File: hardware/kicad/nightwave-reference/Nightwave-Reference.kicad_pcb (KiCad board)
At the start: 4 copper layers, 110 x 100 mm, 61 parts, among them J1 USB4105-GF-A, J2 BATTERY_1S_10050mAh, J3 EXTERNAL_10K_NTC, J4 Molex 104031-0811, J5 SJ-3523-SMT-TR, J6 CMS-28528N-L152, J7 Waveshare 24382 TFT, J8 UART0_SERVICE, SW1 PREV, SW2 PLAY_PAUSE, SW3 NEXT, SW4 VOL_DOWN, SW5 VOL_UP, SW6 MAIN_POWER, U1 ESP32-S3-WROOM-1-N16R8, U10 MAX98357AETE+T, U11 TCA9535PWR, U12 BM83SM1-00TA, U2 TUSB320LAIRWBR, U3 BQ25628ERYKR, U4 TPS22965DSGR, U5 TPS63802DLAR, U6 TPS63802DLAR, U7 MAX17048G+T10, U8 PCM5102APWR, U9 TPA6132A2RTER

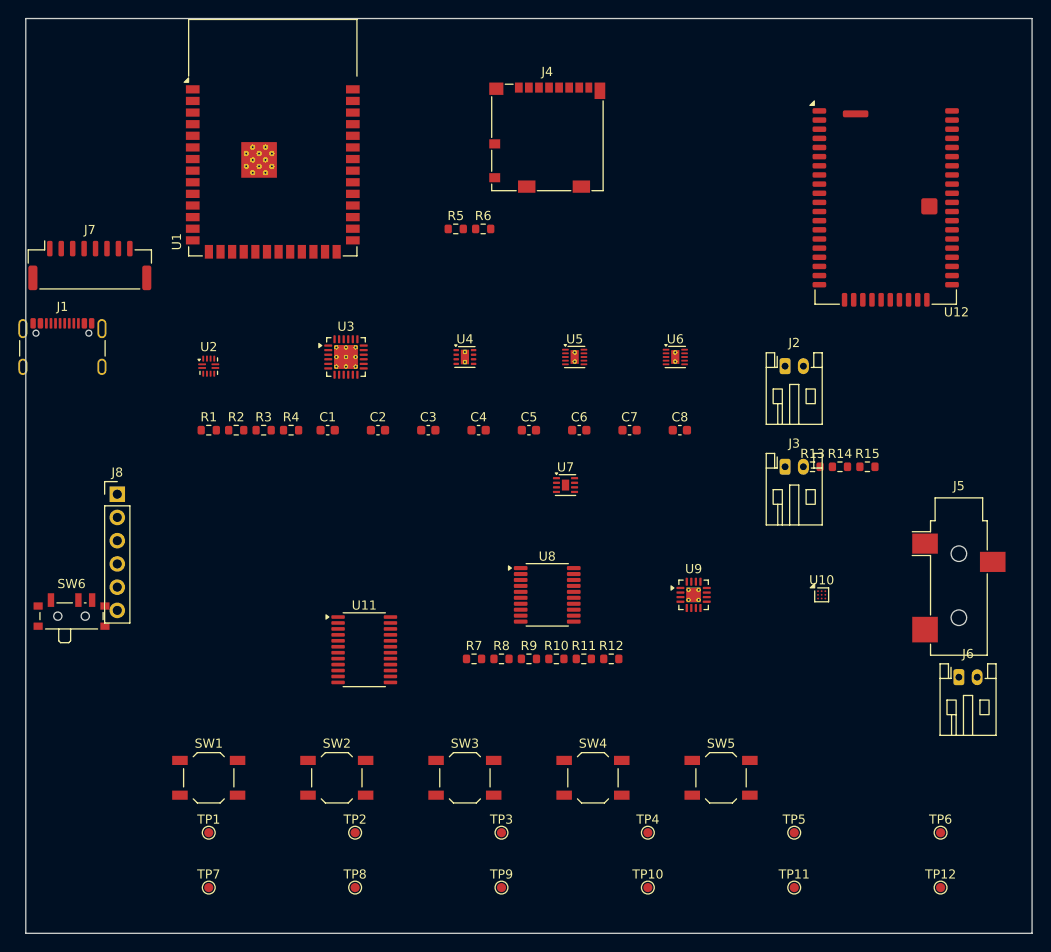
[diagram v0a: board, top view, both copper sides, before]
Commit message: hardware: close reference PCB routing and verify CAD exports
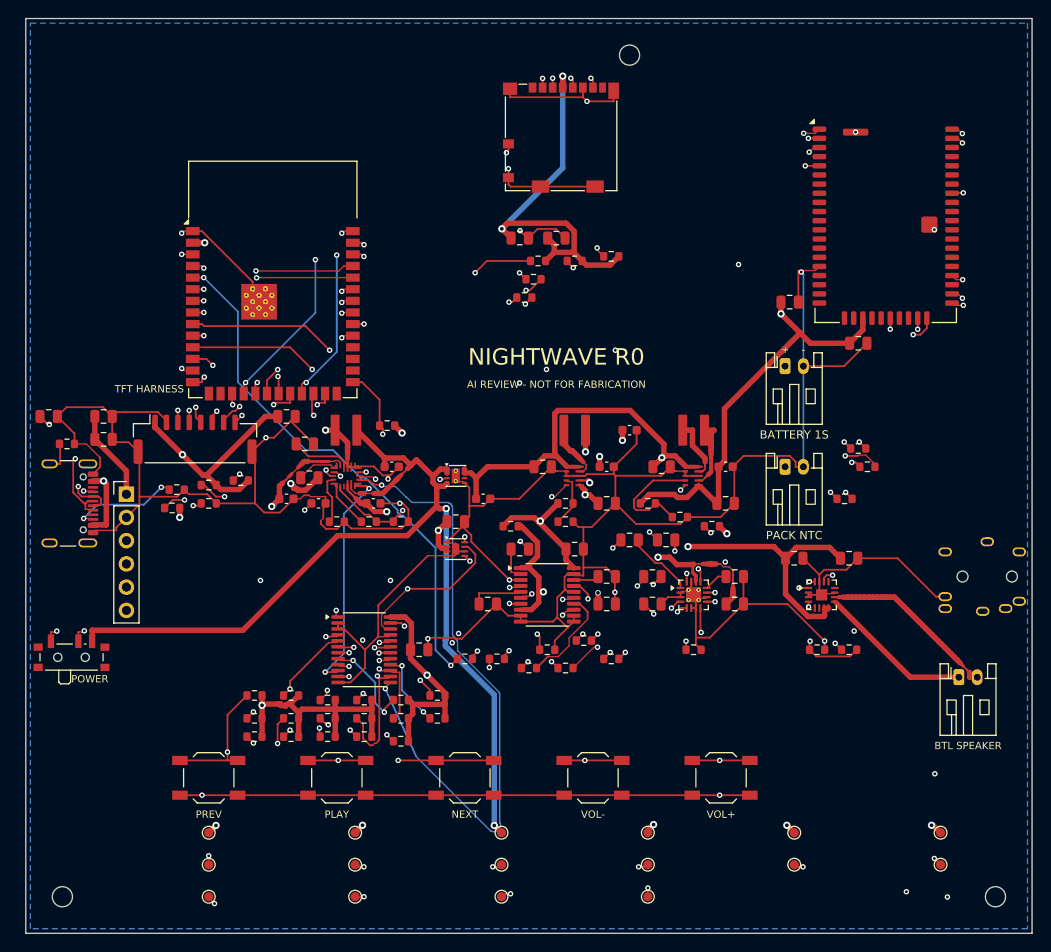
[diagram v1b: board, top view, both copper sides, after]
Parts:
- removed U2: TUSB320LAIRWBR, Package_DFN_QFN:Texas_X2QFN-12_1.6x1.6mm_P0.4mm
- added C10: 10u/25V, Capacitor_SMD:C_0805_2012Metric, F.Cu at (35.5, 51.5)
- added C11: 10u/10V, Capacitor_SMD:C_0805_2012Metric, F.Cu at (61.5, 54.0)
- added C12: 22u/10V, Capacitor_SMD:C_0805_2012Metric, F.Cu at (68.5, 58.0)
- added C13: 10u/10V, Capacitor_SMD:C_0805_2012Metric, F.Cu at (74.5, 54.0)
- added C14: 22u/10V, Capacitor_SMD:C_0805_2012Metric, F.Cu at (81.5, 58.0)
- added C15: 100n/10V, Capacitor_SMD:C_0805_2012Metric, F.Cu at (52.0, 60.0)
- added C16: 100n/10V, Capacitor_SMD:C_0805_2012Metric, F.Cu at (13.5, 51.0)
- added C17: 10u/10V, Capacitor_SMD:C_0805_2012Metric, F.Cu at (13.5, 48.5)
- added C18: 1u/10V, Capacitor_SMD:C_0805_2012Metric, F.Cu at (7.50, 48.5)
- added C19: 100n/10V, Capacitor_SMD:C_0805_2012Metric, F.Cu at (59.0, 29.0)
- added C20: 10u/10V, Capacitor_SMD:C_0805_2012Metric, F.Cu at (63.0, 29.0)
- added C21: 2.2u/10V, Capacitor_SMD:C_0805_2012Metric, F.Cu at (59.0, 63.0)
- added C22: 2.2u/10V, Capacitor_SMD:C_0805_2012Metric, F.Cu at (55.5, 69.0)
- added C23: 100n/10V, Capacitor_SMD:C_0805_2012Metric, F.Cu at (68.5, 66.0)
- added C24: 100n/10V, Capacitor_SMD:C_0805_2012Metric, F.Cu at (68.5, 69.0)
- added C25: 100n/10V, Capacitor_SMD:C_0805_2012Metric, F.Cu at (65.0, 63.0)
- added C26: 1u/10V, Capacitor_SMD:C_0805_2012Metric, F.Cu at (73.5, 66.0)
- added C27: 1u/10V, Capacitor_SMD:C_0805_2012Metric, F.Cu at (73.5, 69.0)
- added C28: 2.2u/10V, Capacitor_SMD:C_0805_2012Metric, F.Cu at (82.5, 66.0)
- added C29: 1u/10V, Capacitor_SMD:C_0805_2012Metric, F.Cu at (71.0, 62.0)
- added C30: 1u/10V, Capacitor_SMD:C_0805_2012Metric, F.Cu at (75.0, 62.0)
- added C31: 100n/10V, Capacitor_SMD:C_0805_2012Metric, F.Cu at (82.5, 69.0)
- added C32: 100n/10V, Capacitor_SMD:C_0805_2012Metric, F.Cu at (89.0, 64.0)
- added C33: 10u/10V, Capacitor_SMD:C_0805_2012Metric, F.Cu at (95.0, 64.0)
- added C34: 100n/10V, Capacitor_SMD:C_0805_2012Metric, F.Cu at (48.0, 74.0)
- added C35: 10u/10V, Capacitor_SMD:C_0805_2012Metric, F.Cu at (33.5, 48.5)
- added C36: 10u/10V, Capacitor_SMD:C_0805_2012Metric, F.Cu at (88.5, 36.0)
- added C37: 100n/10V, Capacitor_SMD:C_0805_2012Metric, F.Cu at (96.0, 40.5)
- added C9: 47n/10V, Capacitor_SMD:C_0805_2012Metric, F.Cu at (36.0, 55.2)
- added H1: M2_NPTH_NYLON_HARDWARE, MountingHole:MountingHole_2.2mm_M2, F.Cu at (71.0, 9.00)
- added H2: M2_NPTH_NYLON_HARDWARE, MountingHole:MountingHole_2.2mm_M2, F.Cu at (9.00, 101.0)
- added H3: M2_NPTH_NYLON_HARDWARE, MountingHole:MountingHole_2.2mm_M2, F.Cu at (111.0, 101.0)
- added L1: 0.47uH XFL4015-471MEC, Nightwave:Coilcraft_XFL4015, F.Cu at (65.0, 50.0)
- added L2: 0.47uH XFL4015-471MEC, Nightwave:Coilcraft_XFL4015, F.Cu at (78.0, 50.0)
- added L3: 0.7uH XFL4015-701MEC, Nightwave:Coilcraft_XFL4015, F.Cu at (40.0, 50.0)
- added R16: 511k, Resistor_SMD:R_0603_1608Metric, F.Cu at (64.0, 58.0)
- added R17: 91k, Resistor_SMD:R_0603_1608Metric, F.Cu at (64.0, 60.0)
- added R18: 562k, Resistor_SMD:R_0603_1608Metric, F.Cu at (73.0, 58.0)
- added R19: 91k, Resistor_SMD:R_0603_1608Metric, F.Cu at (76.5, 59.5)
- added R20: 5.49k, Resistor_SMD:R_0603_1608Metric, F.Cu at (39.0, 60.0)
- added R21: 5.23k, Resistor_SMD:R_0603_1608Metric, F.Cu at (42.5, 60.0)
- added R22: 30.1k, Resistor_SMD:R_0603_1608Metric, F.Cu at (46.0, 60.0)
- added R23: 0, Resistor_SMD:R_0603_1608Metric, F.Cu at (9.50, 51.5)
- added R24: 10k, Resistor_SMD:R_0603_1608Metric, F.Cu at (21.0, 58.5)
- added R25: 10k, Resistor_SMD:R_0603_1608Metric, F.Cu at (44.5, 49.5)
- added R26: 10k, Resistor_SMD:R_0603_1608Metric, F.Cu at (80.0, 60.5)
- added R27: 10k, Resistor_SMD:R_0603_1608Metric, F.Cu at (91.5, 74.0)
- added R28: 10k, Resistor_SMD:R_0603_1608Metric, F.Cu at (78.0, 74.0)
- added R29: 10k, Resistor_SMD:R_0603_1608Metric, F.Cu at (62.0, 74.0)
- added R30: 0, Resistor_SMD:R_0603_1608Metric, F.Cu at (58.0, 60.5)
- added R31: 10k, Resistor_SMD:R_0603_1608Metric, F.Cu at (30.0, 79.0)
- added R32: 10k, Resistor_SMD:R_0603_1608Metric, F.Cu at (34.0, 79.0)
- added R33: 10k, Resistor_SMD:R_0603_1608Metric, F.Cu at (38.0, 79.5)
- added R34: 10k, Resistor_SMD:R_0603_1608Metric, F.Cu at (42.0, 79.5)
- added R35: 10k, Resistor_SMD:R_0603_1608Metric, F.Cu at (46.0, 79.5)
- added R36: 10k, Resistor_SMD:R_0603_1608Metric, F.Cu at (50.0, 79.0)
- added R37: 10k, Resistor_SMD:R_0603_1608Metric, F.Cu at (30.0, 81.5)
- added R38: 10k, Resistor_SMD:R_0603_1608Metric, F.Cu at (34.0, 81.5)
- added R39: 10k, Resistor_SMD:R_0603_1608Metric, F.Cu at (38.0, 81.5)
- added R40: 10k, Resistor_SMD:R_0603_1608Metric, F.Cu at (42.0, 81.5)
- added R41: 10k, Resistor_SMD:R_0603_1608Metric, F.Cu at (46.0, 81.5)
- added R42: 10k, Resistor_SMD:R_0603_1608Metric, F.Cu at (50.0, 81.5)
- added R43: 10k, Resistor_SMD:R_0603_1608Metric, F.Cu at (30.0, 83.5)
- added R44: 10k, Resistor_SMD:R_0603_1608Metric, F.Cu at (34.0, 83.5)
- added R45: 10k, Resistor_SMD:R_0603_1608Metric, F.Cu at (38.0, 83.5)
- added R46: 10k, Resistor_SMD:R_0603_1608Metric, F.Cu at (42.0, 83.5)
- added R47: 10k, Resistor_SMD:R_0603_1608Metric, F.Cu at (46.0, 84.0)
- added R48: 10k, Resistor_SMD:R_0603_1608Metric, F.Cu at (61.0, 31.5)
- added R49: 10k, Resistor_SMD:R_0603_1608Metric, F.Cu at (65.0, 31.5)
- added R50: 10k, Resistor_SMD:R_0603_1608Metric, F.Cu at (69.0, 31.0)
- added R51: 47k, Resistor_SMD:R_0603_1608Metric, F.Cu at (95.0, 74.0)
- added TP13: BT_SERVICE_P34, TestPoint:TestPoint_Pad_D1.0mm, F.Cu at (25.0, 101.0)
- added TP14: BT_LED, TestPoint:TestPoint_Pad_D1.0mm, F.Cu at (41.0, 101.0)
- added TP15: BT_STATE, TestPoint:TestPoint_Pad_D1.0mm, F.Cu at (57.0, 101.0)
- added TP16: HP_DETECT, TestPoint:TestPoint_Pad_D1.0mm, F.Cu at (73.0, 101.0)
- C8: value 1u -> 4.7u
- J2: value BATTERY_1S_10050mAh -> BATTERY_CONNECTOR
- J5: value SJ-3523-SMT-TR -> SJ3-350153AG-TR; footprint Connector_Audio:Jack_3.5mm_CUI_SJ-3523-SMT_Horizontal -> Nightwave:SameSky_SJ3-350153AG
- J6: value CMS-28528N-L152 -> BTL_SPEAKER_CONNECTOR
- J7: value Waveshare 24382 TFT -> TFT_24382_HARNESS
- U10: footprint Package_CSP:WLCSP-9_1.21x1.22mm_Layout3x3_P0.4mm -> Package_DFN_QFN:TQFN-16-1EP_3x3mm_P0.5mm_EP1.23x1.23mm
- U12: footprint RF_Module:Microchip_BM83 -> Nightwave:Microchip_BM83_GroundLands
- U3: footprint Package_DFN_QFN:WQFN-24-1EP_4x4mm_P0.5mm_EP2.6x2.6mm_ThermalVias -> Nightwave:TI_RYK0018A
- U5, U6: footprint Package_DFN_QFN:Texas_DSQ0010A_WSON-10-1EP_2x2mm_P0.4mm_EP0.9x1.5mm_ThermalVias -> Nightwave:TI_DLA0010A
- moved C8 40.3 mm to (37.0, 58.0)
- moved J7 22.2 mm to (23.5, 51.0)
- moved C6 16.5 mm to (81.5, 54.0)
- moved J1 16.0 mm to (8.68, 58.0), turned to -90 degrees
- moved U1 15.5 mm to (32.0, 33.5)
- moved U7 13.9 mm to (52.0, 63.0)
- moved U6 13.2 mm to (78.0, 55.0)
- moved U4 13.0 mm to (52.0, 55.0)
- moved U3 13.0 mm to (40.0, 55.0)
- moved U5 13.0 mm to (65.0, 55.0)
- moved R5 10.6 mm to (59.5, 35.5)
- moved C5 9.39 mm to (68.5, 54.0)
- moved R2 9.19 mm to (21.5, 56.5)
- moved C1 8.75 mm to (33.5, 57.5)
- moved R3 8.49 mm to (25.0, 56.0)
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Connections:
- J1 pad : unconnected-(J1-Pad) -> (no net)
- J4 pad 1: SD_D2_NC -> unconnected-(J4-DAT2-Pad1)
- J4 pad 10: unconnected-(J4-Pad10) -> GND
- J4 pad 2: +3V3 -> SD_DAT3
- J4 pad 8: SD_D1_NC -> unconnected-(J4-DAT1-Pad8)
- J4 pad 9: unconnected-(J4-Pad9) -> SD_DETECT_N
- J5 pad : unconnected-(J5-Pad) -> (no net)
- J7 pad MP: unconnected-(J7-PadMP) -> GND
- SW6 pad : unconnected-(SW6-Pad) -> (no net)
- U1 pad : unconnected-(U1-Pad) -> (no net)
- U1 pad 13: unconnected-(U1-Pad13) -> USB_DM_MCU
- U1 pad 14: unconnected-(U1-Pad14) -> USB_DP_MCU
- U1 pad 36: unconnected-(U1-Pad36) -> UART0_RX
- U1 pad 37: unconnected-(U1-Pad37) -> UART0_TX
- U11 pad 14: USB_INT_N -> PGOOD_CHG
- U12 pad 22: +3V6_BT -> unconnected-(U12-ADAP_IN-Pad22)
- U12 pad 25: +3V3 -> unconnected-(U12-VDD_IO-Pad25)
- U12 pad 46: I2C_SCL -> unconnected-(U12-P1_2/TDI_CPU/SCL-Pad46)
- U12 pad 47: I2C_SDA -> unconnected-(U12-P1_3/TCK_CPU/SDA-Pad47)
- U3 pad 1: VBUS5 -> BTST
- U3 pad 10: TS -> CHG_STAT
- U3 pad 11: ILIM -> CHG_INT_N
- U3 pad 14: CHG_INT_N -> GND
- U3 pad 15: CHG_STAT -> GND
- U3 pad 16: REGN -> SW_CHG
- U3 pad 17: BTST -> PMID
- U3 pad 18: PGND -> VBUS5
- U3 pad 2: PMID -> REGN
- U3 pad 3: SW_CHG -> PGOOD_CHG
- U3 pad 4: SW_CHG -> ILIM
- U3 pad 5: GND -> TS_BIAS
- U3 pad 6: BAT -> TS
- U3 pad 7: BAT -> unconnected-(U3-QON-Pad7)
- U3 pad 8: SYS -> BAT
- U4 pad : unconnected-(U4-Pad) -> (no net)
- U4 pad 4: GND -> SYS
- U4 pad 5: VSYS_SW -> GND
- U4 pad 6: VSYS_SW -> unconnected-(U4-CT-Pad6)
- U5 pad 10: +3V3_EN -> VSYS_SW
- U5 pad 2: SW1_3V3 -> GND
- U5 pad 3: SW2_3V3 -> GND
- U5 pad 4: GND -> FB_3V3
- U5 pad 5: FB_3V3 -> PWR_GOOD_3V3
- U5 pad 7: +3V3 -> SW2_3V3
- U5 pad 8: PWR_GOOD_3V3 -> GND
- U5 pad 9: VSYS_SW -> SW1_3V3
- U6 pad 10: +3V6_BT_EN -> VSYS_SW
- U6 pad 2: SW1_BT -> GND
- U6 pad 3: SW2_BT -> GND
- U6 pad 4: GND -> FB_BT
- U6 pad 5: FB_BT -> PWR_GOOD_BT
- U6 pad 7: +3V6_BT -> SW2_BT
- U6 pad 8: PWR_GOOD_BT -> GND
- U6 pad 9: VSYS_SW -> SW1_BT
- U7 pad : unconnected-(U7-Pad) -> (no net)
- U7 pad 1: BAT -> GND
- U7 pad 2: GND -> BAT
- U7 pad 3: I2C_SCL -> BAT
- U7 pad 4: I2C_SDA -> GND
- U7 pad 6: BAT -> GND
- U7 pad 7: GND -> I2C_SCL
- U7 pad 8: GND -> I2C_SDA
- U8 pad 18: unconnected-(U8-Pad18) -> PCM_LDOO
- U8 pad 2: unconnected-(U8-Pad2) -> PCM_CP_P
- U8 pad 4: unconnected-(U8-Pad4) -> PCM_CP_M
- U8 pad 5: unconnected-(U8-Pad5) -> PCM_VNEG
- U9 pad : unconnected-(U9-Pad) -> (no net)
- U9 pad 1: DAC_L -> HP_IN_L
- U9 pad 11: unconnected-(U9-Pad11) -> HP_CP_P
- U9 pad 12: unconnected-(U9-Pad12) -> HP_VDD
- U9 pad 2: DAC_L -> GND
- U9 pad 3: DAC_R -> GND
- U9 pad 4: DAC_R -> HP_IN_R
- U9 pad 6: unconnected-(U9-Pad6) -> GND
- U9 pad 7: unconnected-(U9-Pad7) -> GND
- U9 pad 8: GND -> HP_VSS
- U9 pad 9: unconnected-(U9-Pad9) -> HP_CP_N
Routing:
- net GND: track 0.00 -> 721.0 mm, vias 0 -> 20
- net +3V3: track 0.00 -> 370.2 mm, vias 0 -> 13
- net I2S_DOUT: track 0.00 -> 178.1 mm, vias 0 -> 6
- net I2S_LRCLK: track 0.00 -> 148.4 mm, vias 0 -> 6
- net BT_SERVICE_P34: track 0.00 -> 146.0 mm, vias 0 -> 3
- net HP_DETECT: track 0.00 -> 145.5 mm, vias 0 -> 5
- net I2S_BCLK: track 0.00 -> 138.2 mm, vias 0 -> 5
- net BT_LED: track 0.00 -> 123.7 mm, vias 0 -> 3
- net BT_STATE: track 0.00 -> 119.3 mm, vias 0 -> 3
- net VSYS_SW: track 0.00 -> 116.0 mm, vias 0 -> 3
- net I2C_SDA: track 0.00 -> 115.7 mm, vias 0 -> 8
- net SYS: track 0.00 -> 111.1 mm, vias 0 -> 2
- net +3V6_BT: track 0.00 -> 110.3 mm, vias 0 -> 2
- net SPK_EN: track 0.00 -> 109.8 mm, vias 0 -> 3
- net BAT: track 0.00 -> 99.0 mm, vias 0 -> 3
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- added copper zone on In2.Cu, net +3V3
- added copper zone on B.Cu, net GND
- added copper zone on In1.Cu, net GND
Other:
- board text added: "+"
- board text added: "-"
- board text added: "AI REVIEW - NOT FOR FABRICATION"
- board text added: "BATTERY 1S"
- board text added: "BTL SPEAKER"
- board text added: "NEXT"
- board text added: "NIGHTWAVE R0"
- board text added: "PACK NTC"
- board text added: "PLAY"
- board text added: "POWER"
- board text added: "PREV"
- board text added: "TFT HARNESS"
- board text added: "VOL+"
- board text added: "VOL-"
